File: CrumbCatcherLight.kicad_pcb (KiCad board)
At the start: 2 copper layers, 79.4 x 91.8 mm, 52 parts, among them J2 Conn_ARM_SWD_TagConnect_TC203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, Q1 2N7002, SW1 SW_SPST, SW10 SW_SPST, SW11 SW_SPST, SW12 SW_SPST, SW14 SW_SPST, SW15 SW_SPST, SW16 SW_SPST, SW17 SW_SPST, SW2 SW_SPST, SW3 SW_SPST, SW4 SW_SPST, SW5 SW_SPST, SW6 SW_SPST, SW7 SW_SPST, SW8 SW_SPST, SW9 SW_SPST, U1 STM32F072CBTx, U2 USBLC6-2SC6

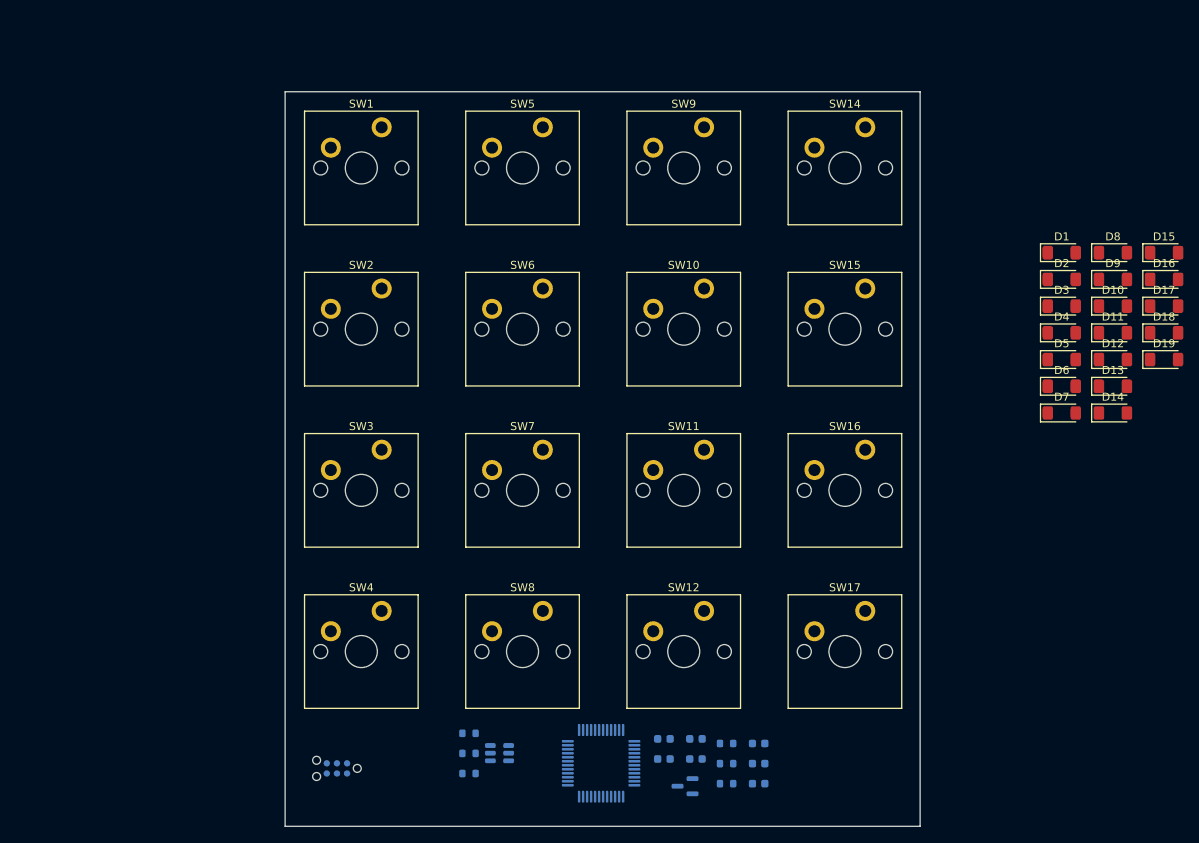
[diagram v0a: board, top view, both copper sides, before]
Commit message: Cleanup, Add usb emc and esd
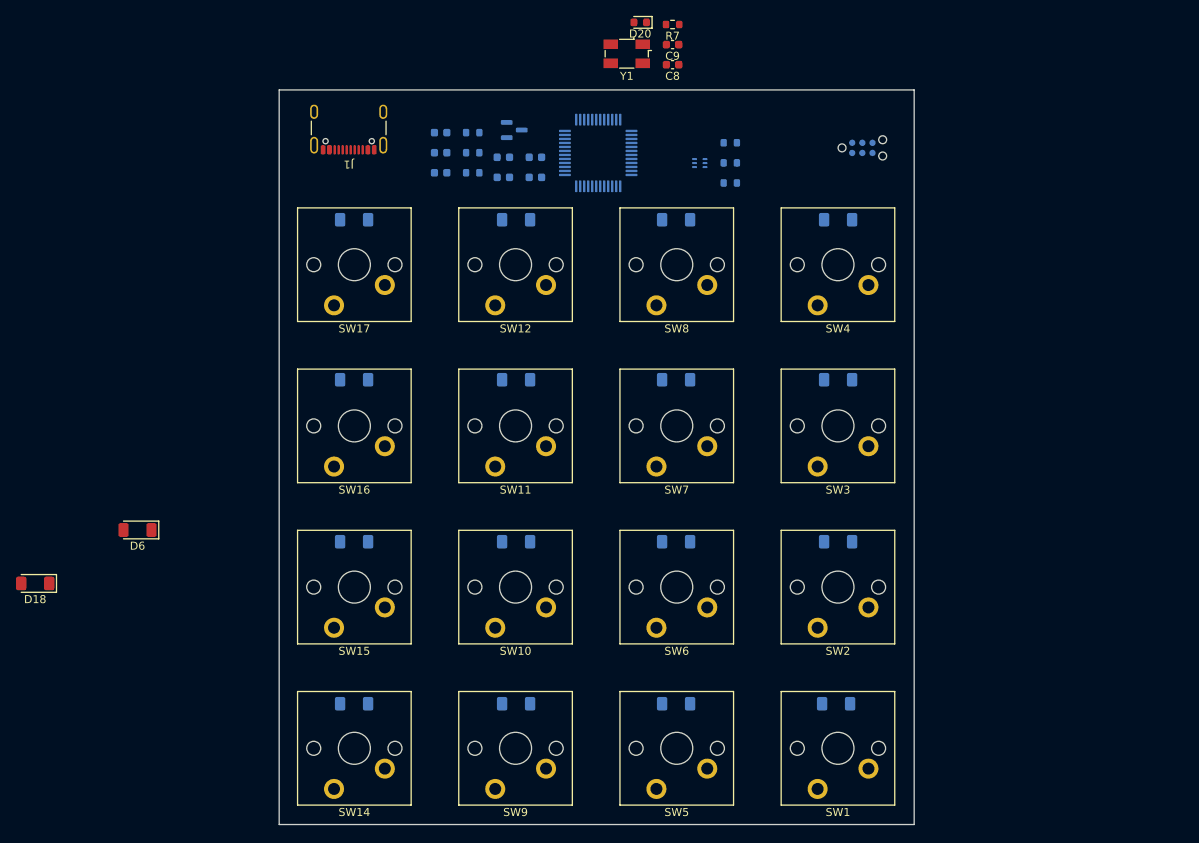
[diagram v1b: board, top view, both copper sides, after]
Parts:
- removed D19: LL4148, Diode_SMD:D_MiniMELF
- added C8: 18pF, Capacitor_SMD:C_0603_1608Metric, F.Cu at (151.2, 46.0)
- added C9: 18pF, Capacitor_SMD:C_0603_1608Metric, F.Cu at (151.2, 43.5)
- added D20: LED RED, LED_SMD:LED_0603_1608Metric, F.Cu at (147.1, 40.7)
- added J1: USB_C_Receptacle_USB2.0, Connector_USB:USB_C_Receptacle_GCT_USB4105-xx-A_16P_TopMnt_Horizontal, F.Cu at (110.7, 53.0)
- added R7: 100R, Resistor_SMD:R_0603_1608Metric, F.Cu at (151.2, 41.0)
- added Y1: 8MHz, Crystal:Crystal_SMD_Abracon_ABM3B-4Pin_5.0x3.2mm, F.Cu at (145.4, 44.6)
- D1, D10, D11, D12, D13, D14, D15, D16, D17, D2, D3, D4, D5, D7, D8, D9: moved to B.Cu
- U2: value USBLC6-2SC6 -> ECMF02-2AMX6; footprint Package_TO_SOT_SMD:SOT-23-6 -> Package_DFN_QFN:ST_UQFN-6L_1.5x1.7mm_P0.5mm
- moved D18 144.5 mm to (71.5, 110.9), turned to 180 degrees
- moved D6 116.9 mm to (84.3, 104.2), turned to 180 degrees
- moved D15 107.5 mm to (111.4, 105.7)
- moved D16 102.0 mm to (111.4, 85.4)
- moved D17 101.8 mm to (111.4, 65.4)
- moved J2 101.6 mm to (174.9, 56.4), turned to 0 degrees
- moved D14 101.6 mm to (111.4, 125.9)
- moved SW14 95.0 mm to (111.4, 131.5), turned to 180 degrees
- moved SW1 93.9 mm to (171.8, 131.5), turned to 180 degrees
- moved C5 90.6 mm to (122.2, 54.5), turned to 0 degrees
- moved D10 89.6 mm to (131.6, 125.9)
- moved R6 87.3 mm to (126.2, 54.5), turned to 0 degrees
- moved C4 86.1 mm to (122.2, 57.0), turned to 0 degrees
- moved R3 85.3 mm to (158.4, 55.8), turned to 0 degrees
- moved Q1 84.7 mm to (131.4, 54.2), turned to 0 degrees
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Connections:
- net /Switches/COL0 renamed Col0
- net /Switches/COL1 renamed Col1
- net /Switches/COL2 renamed Col2
- net /Switches/COL3 renamed Col3
- D1 pad 1: /Switches/ROW0 -> Row1
- D10 pad 1: /Switches/ROW0 -> Row2
- D11 pad 1: /Switches/ROW2 -> Row3
- D12 pad 1: /Switches/ROW3 -> Row4
- D13 pad 1: /Switches/ROW1 -> Row1
- D14 pad 1: /Switches/ROW0 -> Row2
- D15 pad 1: /Switches/ROW1 -> Row3
- D16 pad 1: /Switches/ROW2 -> Row4
- D17 pad 1: /Switches/ROW3 -> Row1
- D18 pad 1: /Switches/ROW0 -> Row3
- D2 pad 1: /Switches/ROW1 -> Row2
- D3 pad 1: /Switches/ROW2 -> Row3
- D4 pad 1: /Switches/ROW3 -> Row4
- D5 pad 1: /Switches/ROW0 -> Row1
- D6 pad 1: /Switches/ROW0 -> Row2
- D6 pad 2: Net-(D5-A) -> Net-(D6-A)
- D7 pad 1: /Switches/ROW1 -> Row3
- D8 pad 1: /Switches/ROW2 -> Row4
- D9 pad 1: /Switches/ROW3 -> Row1
- SW10 pad 1: Net-(D13-A) -> Net-(D10-A)
- SW14 pad 1: Net-(D14-A) -> Net-(D13-A)
- SW15 pad 1: Net-(D15-A) -> Net-(D14-A)
- SW16 pad 1: Net-(D16-A) -> Net-(D15-A)
- SW17 pad 1: Net-(D17-A) -> Net-(D16-A)
- SW6 pad 1: Net-(D8-A) -> Net-(D7-A)
- SW7 pad 1: Net-(D9-A) -> Net-(D8-A)
- SW8 pad 1: Net-(D7-A) -> Net-(D6-A)
- SW9 pad 1: Net-(D10-A) -> Net-(D9-A)
- U2 pad 1: /USB_D+ -> /EXT_USB_D-
- U2 pad 2: GND -> /EXT_USB_D+
- U2 pad 3: /USB_D- -> GND
- U2 pad 4: /EXT_USB_D- -> unconnected-(U2-NC-Pad4)
- U2 pad 5: VBUS -> /USB_D+
- U2 pad 6: /EXT_USB_D+ -> /USB_D-

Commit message: Add LDO and other minor updates
LP38691
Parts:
- removed C8, C9: 18pF, Capacitor_SMD:C_0603_1608Metric
- removed D18, D6: LL4148, Diode_SMD:D_MiniMELF
- removed D20: LED RED, LED_SMD:LED_0603_1608Metric
- removed R7: 100R, Resistor_SMD:R_0603_1608Metric
- removed Y1: 8MHz, Crystal:Crystal_SMD_Abracon_ABM3B-4Pin_5.0x3.2mm

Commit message: Start component selection
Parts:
- removed C7: 100nF, Capacitor_SMD:C_0603_1608Metric
- removed D1: LL4148, Diode_SMD:D_MiniMELF
- removed SW1: SW_SPST, PCM_Switch_Keyboard_Cherry_MX:SW_Cherry_MX_PCB_1.00u
- added C10: 100nF, Capacitor_SMD:C_0402_1005Metric, F.Cu at (130.1, 1.86)
- added C11: 100nF, Capacitor_SMD:C_0402_1005Metric, F.Cu at (143.4, 53.3)
- added C12: 100nF, Capacitor_SMD:C_0402_1005Metric, F.Cu at (130.1, 5.80)
- added C13: 100nF, Capacitor_SMD:C_0402_1005Metric, F.Cu at (133.1, 0.00)
- added C14: 22pF, Capacitor_SMD:C_0402_1005Metric, F.Cu at (119.2, 35.6)
- added C15: 22pF, Capacitor_SMD:C_0402_1005Metric, F.Cu at (119.2, 37.6)
- added C16: 100nF, Capacitor_SMD:C_0402_1005Metric, F.Cu at (133.0, 3.83)
- added C17: 100nF, Capacitor_SMD:C_0402_1005Metric, F.Cu at (133.0, 5.80)
- added C18: 100nF, Capacitor_SMD:C_0402_1005Metric, F.Cu at (136.0, 0.00)
- added C19: 100nF, Capacitor_SMD:C_0402_1005Metric, F.Cu at (136.1, 3.80)
- added C20: 100nF, Capacitor_SMD:C_0402_1005Metric, F.Cu at (136.1, 5.77)
- added C8: 10uF, Capacitor_SMD:C_0402_1005Metric, F.Cu at (202.7, -17.5)
- added C9: 100nF, Capacitor_SMD:C_0402_1005Metric, F.Cu at (130.1, -0.11)
- added D18: LL4148, Diode_SMD:D_MiniMELF, F.Cu at (191.1, 121.3)
- added D19: LL4148, Diode_SMD:D_MiniMELF, F.Cu at (191.1, 124.6)
- added D20: LL4148, Diode_SMD:D_MiniMELF, F.Cu at (202.4, -1.60)
- added D6: LL4148, Diode_SMD:D_MiniMELF, F.Cu at (191.1, 117.9)
- added FB1: BLM15PX330SN1D, Inductor_SMD:L_0402_1005Metric, F.Cu at (120.3, 51.6)
- added R10: 27R, Resistor_SMD:R_0402_1005Metric, F.Cu at (148.2, 32.9)
- added R11: 27R, Resistor_SMD:R_0402_1005Metric, F.Cu at (148.2, 35.4)
- added R12: 1K, Resistor_SMD:R_0402_1005Metric, F.Cu at (122.1, 37.4)
- added R7: 10K, Resistor_SMD:R_0402_1005Metric, F.Cu at (202.7, -7.61)
- added R8: 1K, Resistor_SMD:R_0402_1005Metric, F.Cu at (202.7, -5.62)
- added R9: 1K, Resistor_SMD:R_0402_1005Metric, F.Cu at (144.7, 32.2)
- added SW13: SW_SPST, PCM_Switch_Keyboard_Cherry_MX:SW_Cherry_MX_PCB_1.00u, F.Cu at (171.8, 131.5)
- added TP1: Reset, TestPoint:TestPoint_Pad_D1.0mm, F.Cu at (1.02, 1.02)
- added TP2: Delay, TestPoint:TestPoint_Pad_D1.0mm, F.Cu at (1.02, 4.08)
- added TP3: Boot, TestPoint:TestPoint_Pad_D1.0mm, F.Cu at (1.02, 7.12)
- added U3: GD25LQ128DYIGR, Package_SON:WSON-8-1EP_6x5mm_P1.27mm_EP3.4x4mm, F.Cu at (144.9, 57.3)
- added U4: RP2040, Package_DFN_QFN:QFN-56-1EP_7x7mm_P0.4mm_EP3.2x3.2mm, F.Cu at (154.6, 54.7)
- added Y1: 12MHz, Crystal:Crystal_SMD_Abracon_ABM8G-4Pin_3.2x2.5mm, F.Cu at (115.9, 36.9)
- C1: value 470nF -> 100nF; footprint Capacitor_SMD:C_0603_1608Metric -> Capacitor_SMD:C_0402_1005Metric; moved to F.Cu
- C2: value 4.7uF -> 100nF; footprint Capacitor_SMD:C_0603_1608Metric -> Capacitor_SMD:C_0402_1005Metric; moved to F.Cu
- C3, C4, C5: value 100nF -> 10uF; footprint Capacitor_SMD:C_0603_1608Metric -> Capacitor_SMD:C_0402_1005Metric; moved to F.Cu
- C6: value 100nF -> 4.7uF; footprint Capacitor_SMD:C_0603_1608Metric -> Capacitor_SMD:C_0805_2012Metric; moved to F.Cu
- Q1: value 2N7002 -> 2N7002VC-7; footprint Package_TO_SOT_SMD:SOT-23 -> Package_TO_SOT_SMD:SOT-363_SC-70-6; moved to F.Cu
- R1: value 1M -> 5K1; footprint Resistor_SMD:R_0603_1608Metric -> Resistor_SMD:R_0402_1005Metric
- R2: footprint Resistor_SMD:R_0603_1608Metric -> Resistor_SMD:R_0402_1005Metric
- R3: value 5K1 -> 10K; footprint Resistor_SMD:R_0603_1608Metric -> Resistor_SMD:R_0402_1005Metric; moved to F.Cu
- R4, R6: footprint Resistor_SMD:R_0603_1608Metric -> Resistor_SMD:R_0402_1005Metric; moved to F.Cu
- R5: value 10K -> 51K; footprint Resistor_SMD:R_0603_1608Metric -> Resistor_SMD:R_0402_1005Metric; moved to F.Cu
- U1: value STM32F072CBTx -> ECMF02-2AMX6; footprint Package_QFP:LQFP-48_7x7mm_P0.5mm -> Package_DFN_QFN:ST_UQFN-6L_1.5x1.7mm_P0.5mm; moved to F.Cu
- U2: value ECMF02-2AMX6 -> XC6206PxxxMR-Regulator_Linear; footprint Package_DFN_QFN:ST_UQFN-6L_1.5x1.7mm_P0.5mm -> Package_TO_SOT_SMD:SOT-23; moved to F.Cu
- moved R4 98.2 mm to (199.9, -5.29), turned to 180 degrees
- moved R5 98.2 mm to (199.9, -7.80), turned to 180 degrees
- moved R6 98.2 mm to (199.9, -10.3), turned to 180 degrees
- moved Q1 90.6 mm to (194.7, -10.6), turned to 180 degrees
- moved C6 87.0 mm to (192.1, -4.72), turned to 180 degrees
- moved R3 67.1 mm to (194.7, -0.60), turned to 180 degrees
- moved U2 58.0 mm to (115.2, 15.8), turned to 0 degrees
- moved J2 51.5 mm to (224.9, 44.4)
- moved C4 42.1 mm to (110.6, 16.5), turned to 180 degrees
- moved C5 42.1 mm to (110.6, 14.0), turned to 180 degrees
- moved R2 39.7 mm to (118.7, 58.6)
- moved R1 39.0 mm to (119.8, 55.0)
- moved C1 35.5 mm to (94.5, 58.8), turned to 180 degrees
- moved C2 35.5 mm to (94.5, 56.3), turned to 180 degrees
- moved U1 32.1 mm to (109.8, 59.2), turned to -90 degrees
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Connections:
- C1 pad 1: /STM32/~{RST} -> VBUS
- C1 pad 2: /STM32/GND -> GND
- C2 pad 1: /STM32/BOOT0 -> +5V
- C2 pad 2: Net-(Q1-G) -> GND
- C3 pad 1: /STM32/GND -> +5V
- C3 pad 2: /STM32/3V3 -> GND
- C4 pad 1: /STM32/GND -> +5V
- C4 pad 2: /STM32/3V3 -> GND
- C5 pad 1: /STM32/GND -> IOVDD
- C5 pad 2: /STM32/3V3 -> GND
- C6 pad 1: /STM32/GND -> Net-(Q1B-G)
- C6 pad 2: /STM32/3V3 -> GND
- D10 pad 1: Row2 -> Row1
- D11 pad 1: Row3 -> Row2
- D12 pad 1: Row4 -> Row3
- D13 pad 1: Row1 -> Row4
- D14 pad 1: Row2 -> Row1
- D15 pad 1: Row3 -> Row2
- D16 pad 1: Row4 -> Row3
- D17 pad 1: Row1 -> Row4
- D2 pad 1: Row2 -> Row1
- D3 pad 1: Row3 -> Row2
- D4 pad 1: Row4 -> Row3
- D5 pad 1: Row1 -> Row4
- D7 pad 1: Row3 -> Row2
- D8 pad 1: Row4 -> Row3
- D9 pad 1: Row1 -> Row4
- J1 pad A6: /EXT_USB_D+ -> Net-(U1-D-_in)
- J1 pad A7: /EXT_USB_D- -> Net-(U1-D+_in)
- J1 pad B6: /EXT_USB_D+ -> Net-(U1-D-_in)
- J1 pad B7: /EXT_USB_D- -> Net-(U1-D+_in)
- J1 pad S1: Net-(J1-SHIELD) -> GND
- J2 pad 1: /STM32/3V3 -> IOVDD
- J2 pad 2: /STM32/SWDIO -> /RP2040/SWDIO
- J2 pad 3: /STM32/~{RST} -> /RP2040/~{RST}
- J2 pad 4: /STM32/SWCLK -> /RP2040/SWCLK
- J2 pad 5: /STM32/GND -> GND
- J2 pad 6: /STM32/SWO -> unconnected-(J2-SWO-Pad6)
- Q1 pad 1: Net-(Q1-G) -> GND
- Q1 pad 2: /STM32/GND -> Net-(D20-A)
- Q1 pad 3: /STM32/~{RST} -> GND
- R1 pad 1: Net-(J1-SHIELD) -> Net-(J1-CC1)
- R2 pad 1: Net-(J1-CC1) -> Net-(J1-CC2)
- R3 pad 1: Net-(J1-CC2) -> /RP2040/~{RST}
- R3 pad 2: GND -> IOVDD
- R4 pad 1: /STM32/GND -> GND
- R4 pad 2: /STM32/BOOT0 -> Net-(D20-A)
- R5 pad 1: /STM32/~{RST} -> Net-(Q1B-G)
- R5 pad 2: /STM32/3V3 -> Net-(D20-K)
- R6 pad 1: /STM32/GND -> GND
- R6 pad 2: Net-(Q1-G) -> Net-(Q1B-G)
- SW14 pad 1: Net-(D13-A) -> Net-(D14-A)
- SW15 pad 1: Net-(D14-A) -> Net-(D15-A)
- SW16 pad 1: Net-(D15-A) -> Net-(D16-A)
- SW17 pad 1: Net-(D16-A) -> Net-(D17-A)
- SW5 pad 2: Col1 -> Col0
- SW6 pad 1: Net-(D7-A) -> Net-(D6-A)
- SW8 pad 1: Net-(D6-A) -> Net-(D9-A)
- SW9 pad 1: Net-(D9-A) -> Net-(D7-A)
- SW9 pad 2: Col2 -> Col1
- U1 pad 1: /STM32/3V3 -> Net-(U1-D+_in)
- U1 pad 2: unconnected-(U1-PC13-Pad2) -> Net-(U1-D-_in)
- U1 pad 3: unconnected-(U1-PC14-Pad3) -> GND
- U1 pad 5: /STM32/OSC_IN -> /USB_D+
- U1 pad 6: /STM32/OSC_OUT -> /USB_D-
- U2 pad 1: /EXT_USB_D- -> GND
- U2 pad 2: /EXT_USB_D+ -> IOVDD
- U2 pad 3: GND -> +5V
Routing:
- net /RP2040/QSPI_nCS: track 0.00 -> 13.5 mm
- net /RP2040/QSPI_SD1: track 0.00 -> 11.9 mm
- net /RP2040/QSPI_SD2: track 0.00 -> 10.5 mm
- net GND: track 0.00 -> 10.4 mm, vias 0 -> 1
- net /RP2040/QSPI_SD3: track 0.00 -> 8.85 mm
- net /RP2040/QSPI_SCLK: track 0.00 -> 7.34 mm
- net /RP2040/QSPI_SD0: track 0.00 -> 4.97 mm
- net IOVDD: track 0.00 -> 1.32 mm
